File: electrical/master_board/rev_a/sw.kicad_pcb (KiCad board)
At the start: 2 copper layers, 0 parts

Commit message: Inject the PCB outlines into master/center/ne/nw/se/sw PCB's.
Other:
- board outline added: 64.7 x 45 mm
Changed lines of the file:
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@@
     (uvia_drill 0.1)
   )
+  (gr_line (start 37.50 136.00) (end 29.33 136.00) (layer Edge.Cuts) (width 0.05))
+  (gr_line (start 29.33 136.00) (end 29.20 136.01) (layer Edge.Cuts) (width 0.05))
+  (gr_line (start 29.20 136.01) (end 29.07 136.02) (layer Edge.Cuts) (width 0.05))
+  (gr_line (start 29.07 136.02) (end 28.94 136.05) (layer Edge.Cuts) (width 0.05))
+  (gr_line (start 28.94 136.05) (end 28.81 136.10) (layer Edge.Cuts) (width 0.05))
+  (gr_line (start 28.81 136.10) (end 28.68 136.15) (layer Edge.Cuts) (width 0.05))
+  (gr_line (start 28.68 136.15) (end 28.57 136.21) (layer Edge.Cuts) (width 0.05))
+  (gr_line (start 28.57 136.21) (end 28.45 136.28) (layer Edge.Cuts) (width 0.05))
+  (gr_line (start 28.45 136.28) (end 28.35 136.37) (layer Edge.Cuts) (width 0.05))
+  (gr_line (start 28.35 136.37) (end 28.25 136.46) (layer Edge.Cuts) (width 0.05))
+  (gr_line (start 28.25 136.46) (end 28.16 136.56) (layer Edge.Cuts) (width 0.05))
+  (gr_line (start 28.16 136.56) (end 28.08 136.67) (layer Edge.Cuts) (width 0.05))
+  (gr_line (start 28.08 136.67) (end 28.01 136.79) (layer Edge.Cuts) (width 0.05))
+  (gr_line (start 28.01 136.79) (end 27.96 136.91) (layer Edge.Cuts) (width 0.05))
+  (gr_line (start 27.96 136.91) (end 27.91 137.03) (layer Edge.Cuts) (width 0.05))
+  (gr_line (start 27.91 137.03) (end 27.87 137.16) (layer Edge.Cuts) (width 0.05))
+  (gr_line (start 27.87 137.16) (end 27.85 137.29) (layer Edge.Cuts) (width 0.05))
+  (gr_line (start 27.85 137.29) (end 27.84 137.43) (layer Edge.Cuts) (width 0.05))
+  (gr_line (start 27.84 137.43) (end 27.83 137.56) (layer Edge.Cuts) (width 0.05))
+  (gr_line (start 27.83 137.56) (end 27.85 137.69) (layer Edge.Cuts) (width 0.05))
+  (gr_line (start 27.85 137.69) (end 27.87 137.83) (layer Edge.Cuts) (width 0.05))
+  (gr_line (start 27.87 137.83) (end 27.90 137.96) (layer Edge.Cuts) (width 0.05))
+  (gr_line (start 27.90 137.96) (end 27.95 138.08) (layer Edge.Cuts) (width 0.05))
+  (gr_line (start 27.95 138.08) (end 28.01 138.20) (layer Edge.Cuts) (width 0.05))
+  (gr_line (start 28.01 138.20) (end 28.01 138.20) (layer Edge.Cuts) (width 0.05))
+  (gr_line (start 28.01 138.20) (end 31.65 144.40) (layer Edge.Cuts) (width 0.05))
+  (gr_line (start 31.65 144.40) (end 35.83 150.24) (layer Edge.Cuts) (width 0.05))
+  (gr_line (start 35.83 150.24) (end 40.50 155.70) (layer Edge.Cuts) (width 0.05))
+  (gr_line (start 40.50 155.70) (end 45.64 160.72) (layer Edge.Cuts) (width 0.05))
+  (gr_line (start 45.64 160.72) (end 51.20 165.28) (layer Edge.Cuts) (width 0.05))
+  (gr_line (start 51.20 165.28) (end 57.14 169.32) (layer Edge.Cuts) (width 0.05))
+  (gr_line (start 57.14 169.32) (end 63.41 172.83) (layer Edge.Cuts) (width 0.05))
+  (gr_line (start 63.41 172.83) (end 69.97 175.77) (layer Edge.Cuts) (width 0.05))
+  (gr_line (start 69.97 175.77) (end 76.76 178.12) (layer Edge.Cuts) (width 0.05))
+  (gr_line (start 76.76 178.12) (end 83.73 179.86) (layer Edge.Cuts) (width 0.05))
+  (gr_line (start 83.73 179.86) (end 90.83 180.98) (layer Edge.Cuts) (width 0.05))
+  (gr_line (start 90.83 180.98) (end 90.96 180.99) (layer Edge.Cuts) (width 0.05))
+  (gr_line (start 90.96 180.99) (end 91.10 180.99) (layer Edge.Cuts) (width 0.05))
+  (gr_line (start 91.10 180.99) (end 91.23 180.97) (layer Edge.Cuts) (width 0.05))
+  (gr_line (start 91.23 180.97) (end 91.36 180.95) (layer Edge.Cuts) (width 0.05))
+  (gr_line (start 91.36 180.95) (end 91.49 180.91) (layer Edge.Cuts) (width 0.05))
+  (gr_line (start 91.49 180.91) (end 91.61 180.86) (layer Edge.Cuts) (width 0.05))
+  (gr_line (start 91.61 180.86) (end 91.73 180.80) (layer Edge.Cuts) (width 0.05))
+  (gr_line (start 91.73 180.80) (end 91.84 180.73) (layer Edge.Cuts) (width 0.05))
+  (gr_line (start 91.84 180.73) (end 91.95 180.65) (layer Edge.Cuts) (width 0.05))
+  (gr_line (start 91.95 180.65) (end 92.05 180.57) (layer Edge.Cuts) (width 0.05))
+  (gr_line (start 92.05 180.57) (end 92.14 180.47) (layer Edge.Cuts) (width 0.05))
+  (gr_line (start 92.14 180.47) (end 92.22 180.36) (layer Edge.Cuts) (width 0.05))
+  (gr_line (start 92.22 180.36) (end 92.29 180.25) (layer Edge.Cuts) (width 0.05))
+  (gr_line (start 92.29 180.25) (end 92.36 180.14) (layer Edge.Cuts) (width 0.05))
+  (gr_line (start 92.36 180.14) (end 92.41 180.01) (layer Edge.Cuts) (width 0.05))
+  (gr_line (start 92.41 180.01) (end 92.45 179.89) (layer Edge.Cuts) (width 0.05))
+  (gr_line (start 92.45 179.89) (end 92.48 179.76) (layer Edge.Cuts) (width 0.05))
+  (gr_line (start 92.48 179.76) (end 92.49 179.62) (layer Edge.Cuts) (width 0.05))
+  (gr_line (start 92.49 179.62) (end 92.50 179.49) (layer Edge.Cuts) (width 0.05))
+  (gr_line (start 92.50 179.49) (end 92.50 158.60) (layer Edge.Cuts) (width 0.05))
+  (gr_line (start 92.50 158.60) (end 54.00 158.60) (layer Edge.Cuts) (width 0.05))
+  (gr_line (start 54.00 158.60) (end 47.85 153.20) (layer Edge.Cuts) (width 0.05))
+  (gr_line (start 47.85 153.20) (end 42.33 147.16) (layer Edge.Cuts) (width 0.05))
+  (gr_line (start 42.33 147.16) (end 37.50 140.55) (layer Edge.Cuts) (width 0.05))
+  (gr_line (start 37.50 140.55) (end 37.50 136.00) (layer Edge.Cuts) (width 0.05))
 )

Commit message: Finally have everything fitting together.
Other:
- outline, holes or cut-outs redrawn
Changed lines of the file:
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@@
   (gr_line (start 92.48 179.76) (end 92.49 179.62) (layer Edge.Cuts) (width 0.05))
   (gr_line (start 92.49 179.62) (end 92.5 179.49) (layer Edge.Cuts) (width 0.05))
-  (gr_line (start 92.5 179.49) (end 92.5 158.6) (layer Edge.Cuts) (width 0.05))
-  (gr_line (start 92.5 158.6) (end 54 158.6) (layer Edge.Cuts) (width 0.05))
-  (gr_line (start 54 158.6) (end 47.85 153.2) (layer Edge.Cuts) (width 0.05))
-  (gr_line (start 47.85 153.2) (end 42.33 147.16) (layer Edge.Cuts) (width 0.05))
-  (gr_line (start 42.33 147.16) (end 37.5 140.55) (layer Edge.Cuts) (width 0.05))
+  (gr_line (start 92.5 179.49) (end 92.5 159.1) (layer Edge.Cuts) (width 0.05))
+  (gr_line (start 92.5 159.1) (end 54.64 159.1) (layer Edge.Cuts) (width 0.05))
+  (gr_line (start 54.64 159.1) (end 48.24 153.58) (layer Edge.Cuts) (width 0.05))
+  (gr_line (start 48.24 153.58) (end 42.5 147.37) (layer Edge.Cuts) (width 0.05))
+  (gr_line (start 42.5 147.37) (end 37.5 140.55) (layer Edge.Cuts) (width 0.05))
   (gr_line (start 37.5 140.55) (end 37.5 136) (layer Edge.Cuts) (width 0.05))
 )

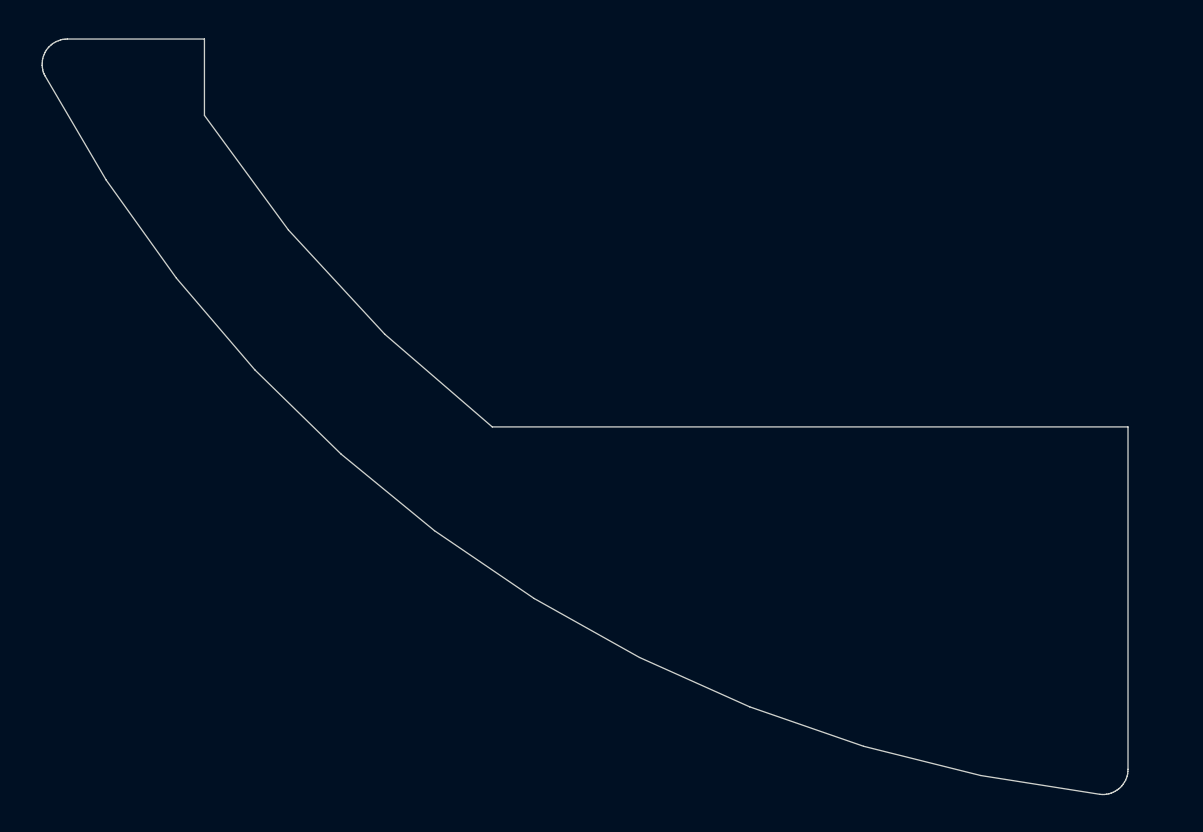
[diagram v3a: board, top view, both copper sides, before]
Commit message: Added spacer mounting holes to schematics and associated PCB's.
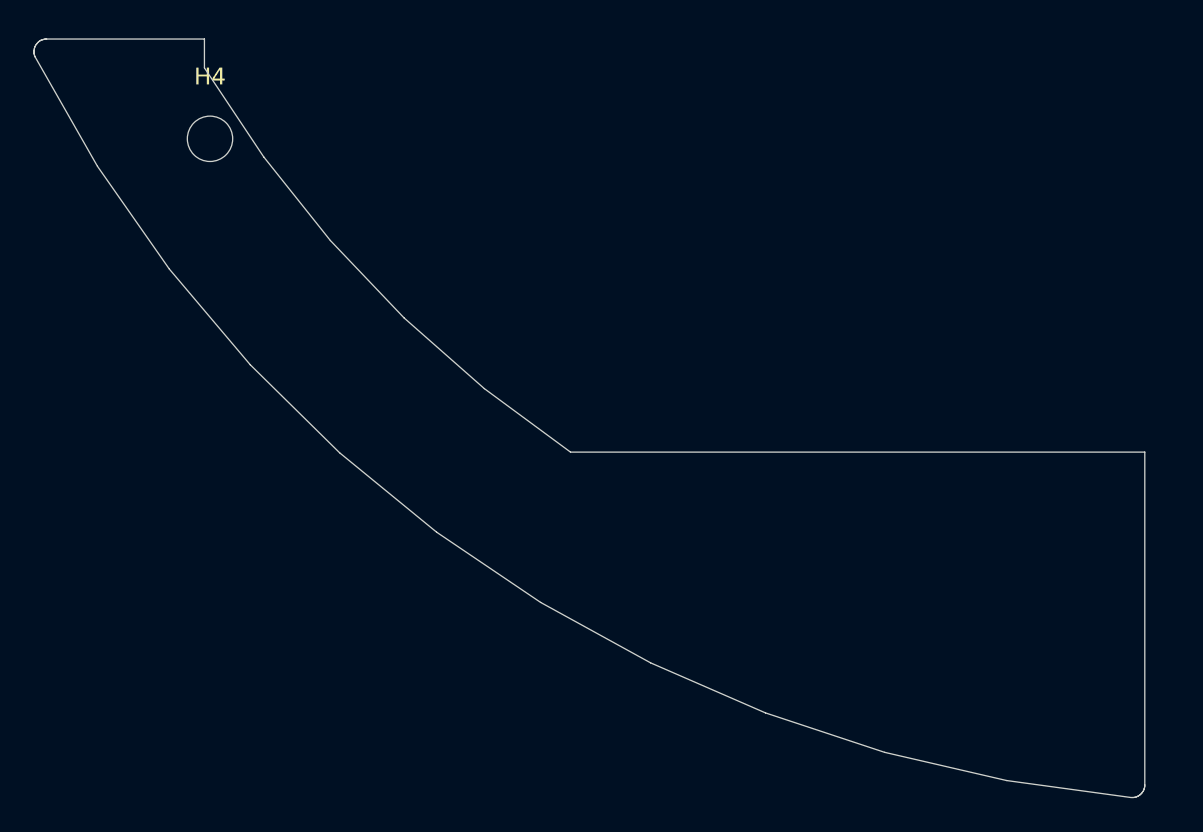
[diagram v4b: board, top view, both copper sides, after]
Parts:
- added H4: HOLE;M2.5, MountingHole:MountingHole_2.7mm_M2.5, F.Cu at (37.8, 141.9)
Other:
- board size 64.7 x 45 mm -> 66.2 x 45.2 mm

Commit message: Added LED's to the PCB's.
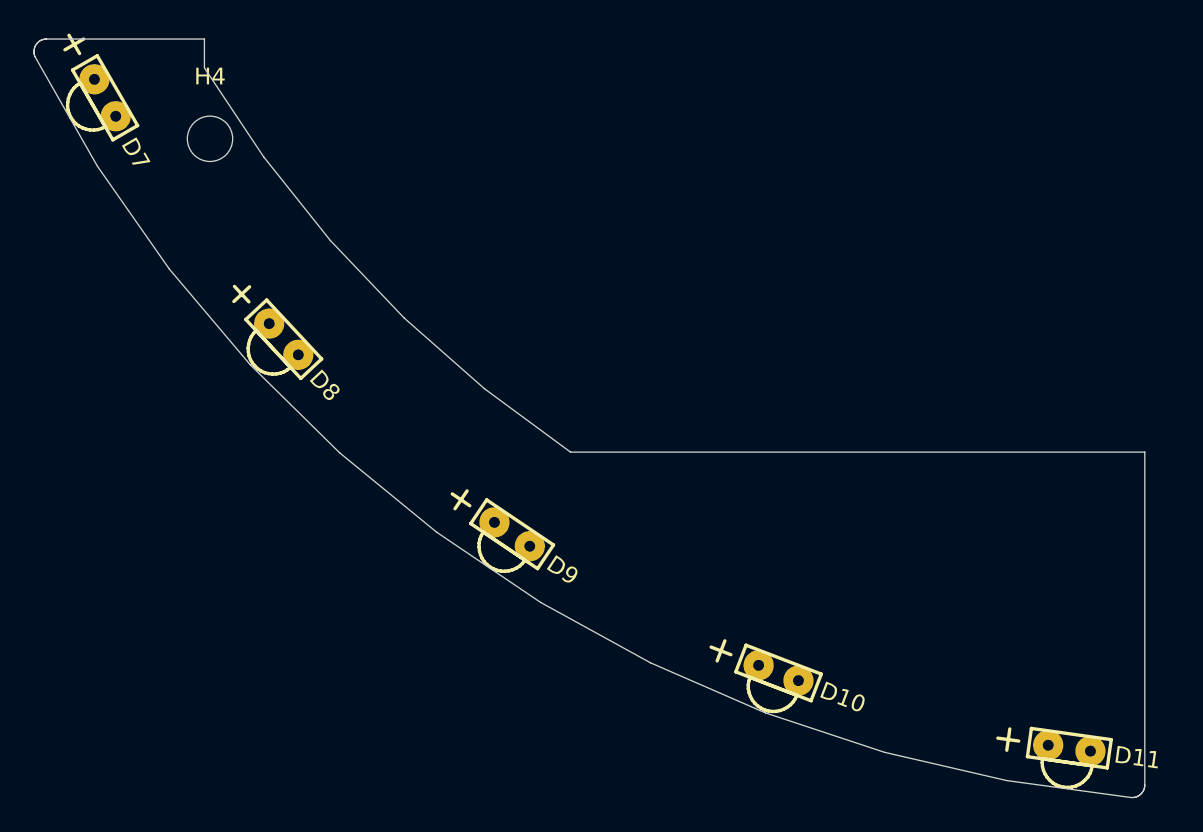
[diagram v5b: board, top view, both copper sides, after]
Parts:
- added D10: LED;GRNRA, HR2:LED_GRNRA, F.Cu at (71.7, 173.8)
- added D11: LED;GRNRA, HR2:LED_GRNRA, F.Cu at (89.0, 178.2)
- added D7: LED;GRNRA, HR2:LED_GRNRA, F.Cu at (31.6, 139.5)
- added D8: LED;GRNRA, HR2:LED_GRNRA, F.Cu at (42.2, 153.9)
- added D9: LED;GRNRA, HR2:LED_GRNRA, F.Cu at (55.8, 165.5)

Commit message: Got Bridge connectors installed on PCB's. Tweaking still required.
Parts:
- added CN108: BRIDGE_SW_OUTER;M1x8, HR2:BRIDGE_SW_OUTER_M1x8, F.Cu at (82.0, 161.9)

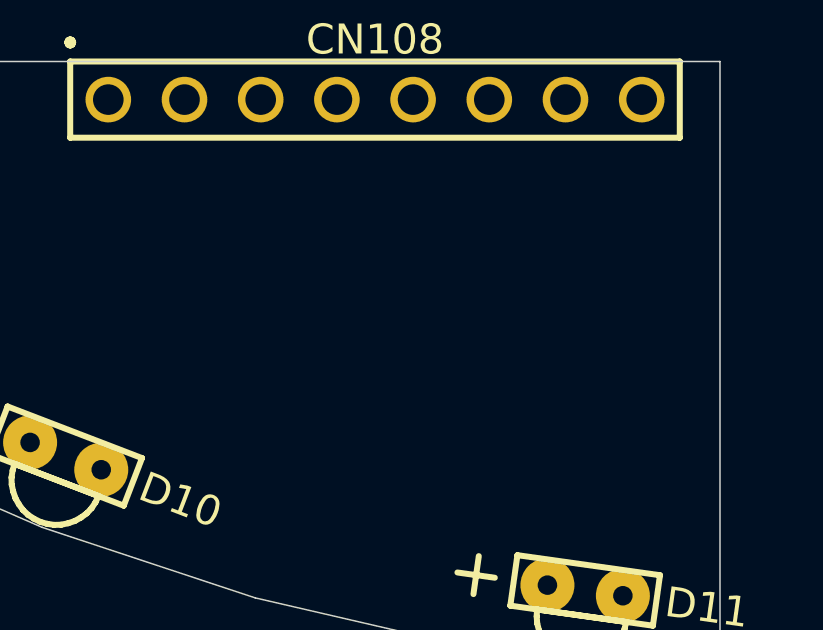
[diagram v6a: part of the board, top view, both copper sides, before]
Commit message: Started working on zones. (Added zone to sw.pro)
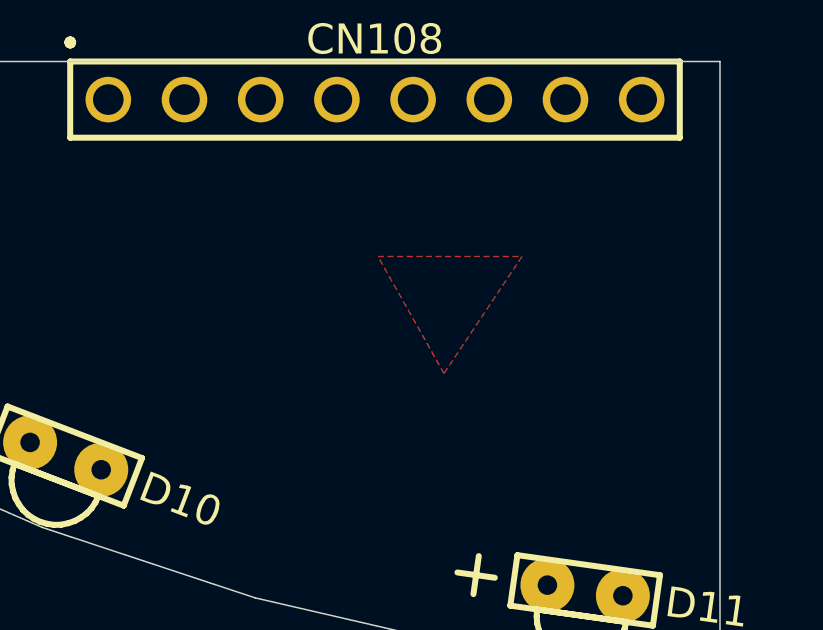
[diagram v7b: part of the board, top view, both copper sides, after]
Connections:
- net Net-(CN108-Pad1) renamed /GND
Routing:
- added copper zone on F.Cu, net /GND

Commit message: More zone testing.
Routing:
- added copper zone on B.Cu, net /GND
